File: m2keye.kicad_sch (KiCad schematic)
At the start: 17 parts, among them J100 Bus_M.2_2199230-2

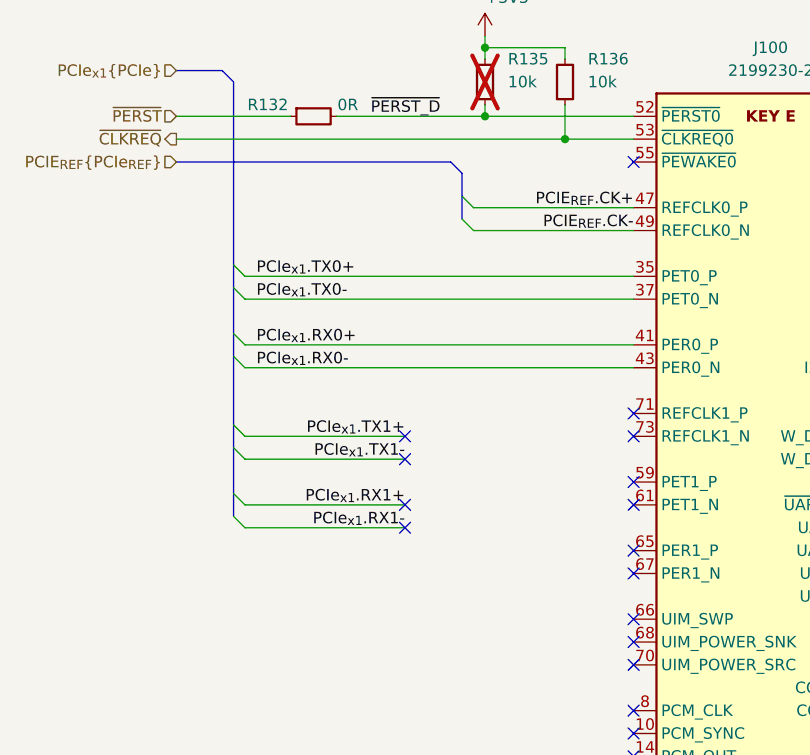
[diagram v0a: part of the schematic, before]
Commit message: [#70030] Routed PCIe
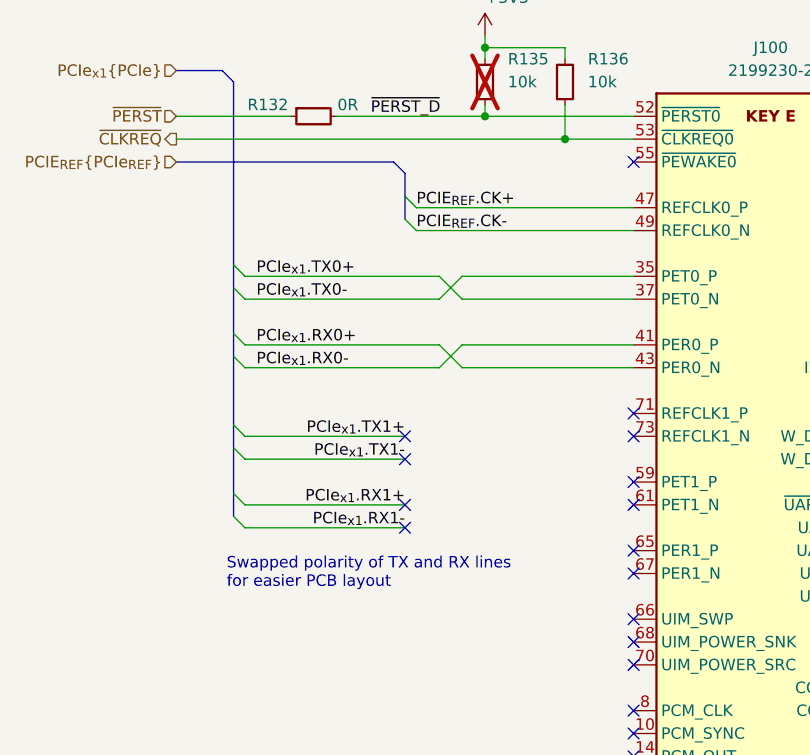
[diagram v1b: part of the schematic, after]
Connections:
- net PCIe_{x1}.RX0+: now also J100.43 (PER0_N); no longer J100.41 (PER0_P)
- net PCIe_{x1}.RX0-: now also J100.41 (PER0_P); no longer J100.43 (PER0_N)
- net PCIe_{x1}.TX0+: now also J100.37 (PET0_N); no longer J100.35 (PET0_P)
- net PCIe_{x1}.TX0-: now also J100.35 (PET0_P); no longer J100.37 (PET0_N)
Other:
- note added: "Swapped polarity of TX and RX lines for easier PCB layout"
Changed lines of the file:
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@@
 	)
 	(bus_entry
-		(at 165.1 92.71)
+		(at 158.75 92.71)
 		(size -1.27 -1.27)
 		(stroke
@@
 	)
 	(bus_entry
-		(at 165.1 95.25)
+		(at 158.75 95.25)
 		(size -1.27 -1.27)
 		(stroke
@@
 	(wire
 		(pts
-			(xy 139.7 100.33) (xy 182.88 100.33)
+			(xy 139.7 100.33) (xy 161.29 100.33)
 		)
 		(stroke
@@
 	(bus
 		(pts
-			(xy 162.56 87.63) (xy 132.08 87.63)
+			(xy 156.21 87.63) (xy 132.08 87.63)
 		)
 		(stroke
@@
 	(bus
 		(pts
-			(xy 163.83 88.9) (xy 162.56 87.63)
+			(xy 157.48 88.9) (xy 156.21 87.63)
 		)
 		(stroke
@@
 	(bus
 		(pts
-			(xy 163.83 93.98) (xy 163.83 91.44)
+			(xy 157.48 93.98) (xy 157.48 91.44)
 		)
 		(stroke
@@
 	(wire
 		(pts
-			(xy 182.88 95.25) (xy 165.1 95.25)
+			(xy 182.88 95.25) (xy 158.75 95.25)
 		)
 		(stroke
@@
 	(wire
 		(pts
+			(xy 163.83 100.33) (xy 161.29 102.87)
+		)
+		(stroke
+			(width 0)
+			(type default)
+		)
+	)
+	(wire
+		(pts
 			(xy 247.65 165.1) (xy 247.65 172.72)
 		)
@@
 	(wire
 		(pts
+			(xy 163.83 100.33) (xy 182.88 100.33)
+		)
+		(stroke
+			(width 0)
+			(type default)
+		)
+	)
+	(wire
+		(pts
 			(xy 157.48 118.11) (xy 139.7 118.11)
 		)
@@
 	(wire
 		(pts
+			(xy 163.83 107.95) (xy 161.29 110.49)
+		)
+		(stroke
+			(width 0)
+			(type default)
+		)
+	)
+	(wire
+		(pts
 			(xy 175.26 85.09) (xy 182.88 85.09)
 		)
@@
 	(wire
 		(pts
+			(xy 161.29 107.95) (xy 163.83 110.49)
+		)
+		(stroke
+			(width 0)
+			(type default)
+		)
+	)
+	(wire
+		(pts
 			(xy 227.33 95.25) (xy 237.49 95.25)
 		)
@@
 	(wire
 		(pts
+			(xy 161.29 110.49) (xy 139.7 110.49)
+		)
+		(stroke
+			(width 0)
+			(type default)
+		)
+	)
+	(wire
+		(pts
 			(xy 234.95 158.75) (xy 234.95 160.02)
 		)
@@
 	(wire
 		(pts
-			(xy 182.88 92.71) (xy 165.1 92.71)
+			(xy 182.88 92.71) (xy 158.75 92.71)
 		)
 		(stroke
@@
 		)
 	)
+	(wire
+		(pts
+			(xy 163.83 102.87) (xy 182.88 102.87)
+		)
+		(stroke
+			(width 0)
+			(type default)
+		)
+	)
 	(bus
 		(pts
@@
 	(wire
 		(pts
-			(xy 182.88 110.49) (xy 139.7 110.49)
+			(xy 161.29 100.33) (xy 163.83 102.87)
+		)
+		(stroke
+			(width 0)
+			(type default)
+		)
+	)
+	(wire
+		(pts
+			(xy 182.88 110.49) (xy 163.83 110.49)
 		)
 		(stroke
@@
 	(bus
 		(pts
-			(xy 163.83 91.44) (xy 163.83 88.9)
+			(xy 157.48 91.44) (xy 157.48 88.9)
 		)
 		(stroke
@@
 	(wire
 		(pts
+			(xy 161.29 107.95) (xy 139.7 107.95)
+		)
+		(stroke
+			(width 0)
+			(type default)
+		)
+	)
+	(wire
+		(pts
 			(xy 166.37 74.93) (xy 166.37 76.2)
 		)
@@
 	(wire
 		(pts
-			(xy 182.88 107.95) (xy 139.7 107.95)
+			(xy 182.88 107.95) (xy 163.83 107.95)
 		)
 		(stroke
@@
 	(wire
 		(pts
-			(xy 139.7 102.87) (xy 182.88 102.87)
+			(xy 139.7 102.87) (xy 161.29 102.87)
 		)
 		(stroke
@@
 		)
 	)
+	(text "Swapped polarity of TX and RX lines\nfor easier PCB layout"
+		(exclude_from_sim no)
+		(at 137.668 135.128 0)
+		(effects
+			(font
+				(size 1.27 1.27)
+			)
+			(justify left bottom)
+		)
+	)
 	(label "~{LED_1}"
 		(at 218.44 167.64 0)
@@
 	)
 	(label "PCIE_{REF}.CK-"
-		(at 182.88 95.25 180)
-		(fields_autoplaced yes)
-		(effects
-			(font
-				(size 1.27 1.27)
-			)
-			(justify right bottom)
+		(at 158.75 95.25 0)
+		(fields_autoplaced yes)
+		(effects
+			(font
+				(size 1.27 1.27)
+			)
+			(justify left bottom)
 		)
 	)
@@
 	)
 	(label "PCIE_{REF}.CK+"
-		(at 182.88 92.71 180)
-		(fields_autoplaced yes)
-		(effects
-			(font
-				(size 1.27 1.27)
-			)
-			(justify right bottom)
-		)
-	)
+		(at 158.75 92.71 0)
+		(fields_autoplaced yes)
+		(effects
+			(font
+				(size 1.27 1.27)
+			)
+			(justify left bottom)
+		)
+	)

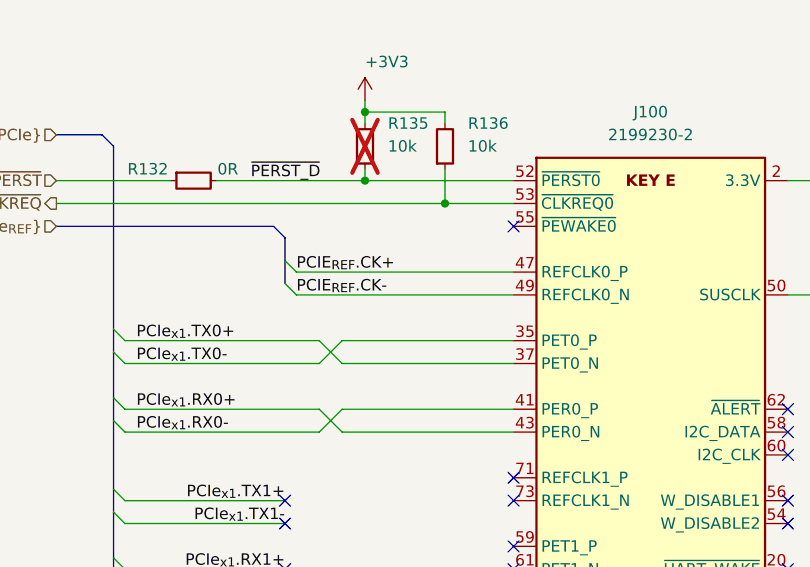
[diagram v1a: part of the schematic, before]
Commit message: [#70030] Connected all the signals
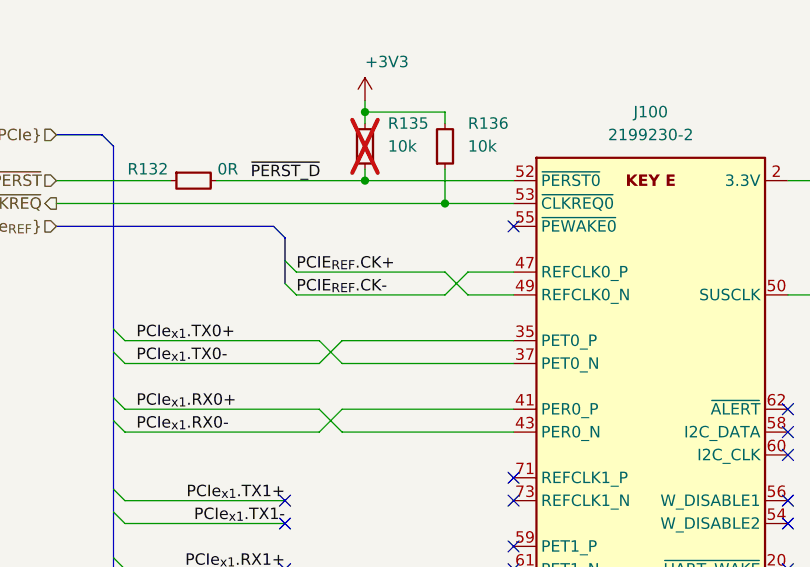
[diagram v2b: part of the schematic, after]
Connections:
- net PCIE_{REF}.CK+: now also J100.49 (REFCLK0_N); no longer J100.47 (REFCLK0_P)
- net PCIE_{REF}.CK-: now also J100.47 (REFCLK0_P); no longer J100.49 (REFCLK0_N)
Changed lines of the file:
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@@
+	(wire
+		(pts
+			(xy 175.26 95.25) (xy 158.75 95.25)
+		)
+		(stroke
+			(width 0)
+			(type default)
+		)
+	)
 	(wire
 		(pts
@@
 	(wire
 		(pts
-			(xy 182.88 95.25) (xy 158.75 95.25)
+			(xy 182.88 95.25) (xy 177.8 95.25)
 		)
 		(stroke
@@
 	(wire
 		(pts
+			(xy 175.26 92.71) (xy 158.75 92.71)
+		)
+		(stroke
+			(width 0)
+			(type default)
+		)
+	)
+	(wire
+		(pts
 			(xy 163.83 107.95) (xy 161.29 110.49)
 		)
@@
 	(wire
 		(pts
-			(xy 182.88 92.71) (xy 158.75 92.71)
+			(xy 182.88 92.71) (xy 177.8 92.71)
 		)
 		(stroke
@@
 	(wire
 		(pts
+			(xy 175.26 92.71) (xy 177.8 95.25)
+		)
+		(stroke
+			(width 0)
+			(type default)
+		)
+	)
+	(wire
+		(pts
 			(xy 175.26 81.28) (xy 175.26 85.09)
 		)
 		(stroke
+			(width 0)
+			(type default)
+		)
+	)
+	(wire
+		(pts
+			(xy 177.8 92.71) (xy 175.26 95.25)
+		)
+		(stroke
